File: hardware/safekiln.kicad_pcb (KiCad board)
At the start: 2 copper layers, 100 x 70 mm, 125 parts, among them J1 5V DC IN, J10 CT 30A/1V, J11 UART / EXPANSION, J2 USB-C, J3 TC1 KILN (K), J4 Conn_ARM_SWD_TagConnect_TC2030, J5 OLED 128x64 I2C, J6 SSR CTRL, J7 TC2 KILN (K), J8 CONTACTOR COIL 5V, J9 LID SWITCH, Q1 AO3400A, Q3 AO3400A, Q4 AO3400A, Q5 AO3400A, SW1 RESET, SW2 BOOT, SW3 ENCODER, U1 ESP32-S3-WROOM-1, U2 AMS1117-3.3, U3 MAX31856, U4 MAX31856, U5 STM32G031K8Tx

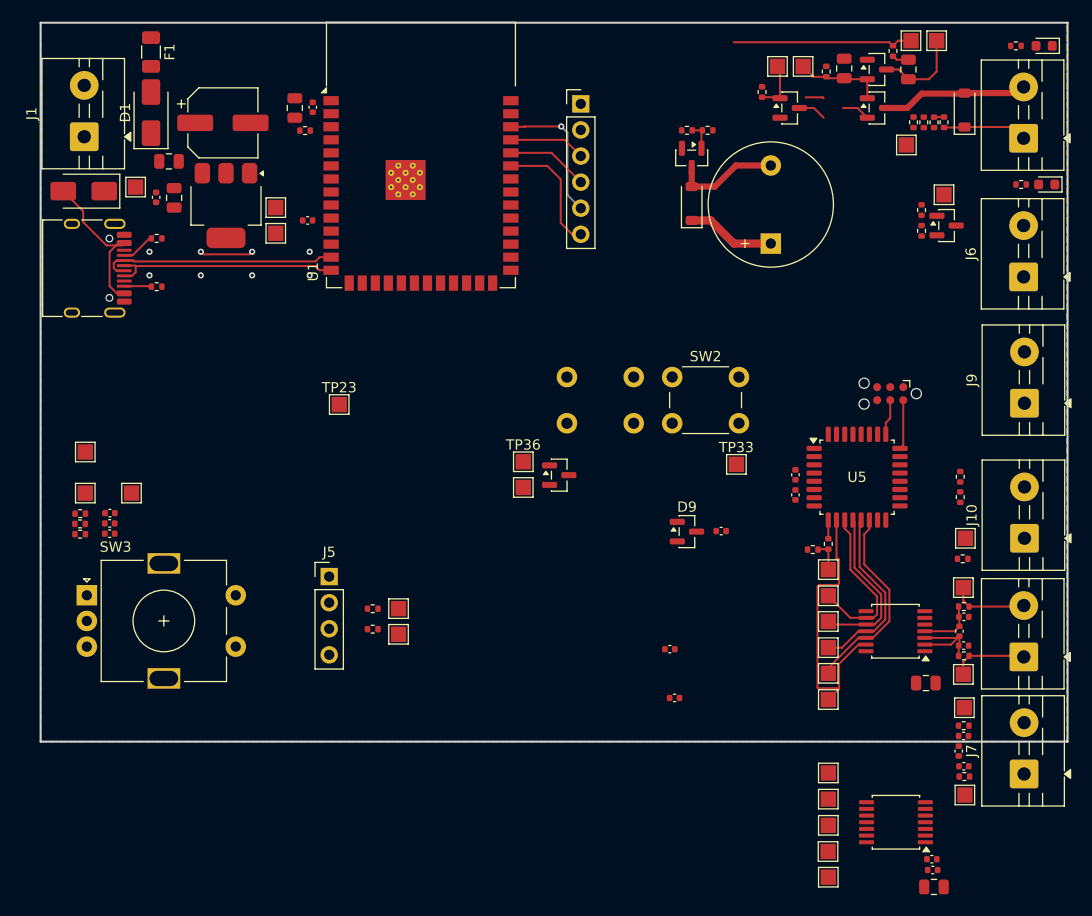
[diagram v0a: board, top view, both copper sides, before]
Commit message: feat: a part number on every bom line, and the buttons go surface mount
Includes the J3/J7 split made in the editor: the two thermocouples are two
2-position blocks again rather than one 4-way, which is what the catalogue
actually stocks. LCSC lists KF301-5.0 in 2P and 3P and no 4P, so the
consolidated connector was a part nobody could order.

All 90 BOM lines now carry an LCSC number, 34 distinct, with the 34 test
points and J4 excluded as the bare pads they are rather than appearing as
lines a BOM cannot fulfil. Three defects came out of doing it:

  R6 and R7 both carried C25076, which is a 100R resistor, while R6 is 220R
  and R7 is 10k. R7 is the pull-up in the supervisor's TX network, so 100R
  would have drawn 33 mA and left R6 no longer limiting anything. One part
  number had propagated onto three different resistance values by field copy.
  Now C25091 and C25744.

  J7 kept J3's value when it was copied, so both thermocouple blocks read
  TC1, on the BOM and on the silkscreen, for a board whose two couples are
  the thing the supervisor cross-checks.

  The 34 test points were (in_bom yes).

Nothing caught any of that because there is no hardware gate in CI at all:
no ERC, no DRC, no BOM check. ERC is clean today at --severity-all with no
exclusions, and tools/fetch3d.py --check verifies the models, so a job
running both plus "every BOM line has an LCSC" and "no part number against
two values" would hold the line at no cost. Tracked as A33.

SW1, SW2 and BZ1 are surface mount. The switches go to the XKB TS-1187A
(C318884), whose footprint KiCad already ships, and neither switch net was
routed yet, so the swap cost no rework. The low-profile 1.5 mm variant is
deliberate: these are service controls, and while RESET also clears the
supervisor's trip latch through D4 (A27), making it easier to press by
accident would be a step backwards.

BZ1 goes to the FST-9650B-5V (C391033), which keeps SYS-HW-09 as written:
active with built-in drive, magnetic, 5 V, and th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
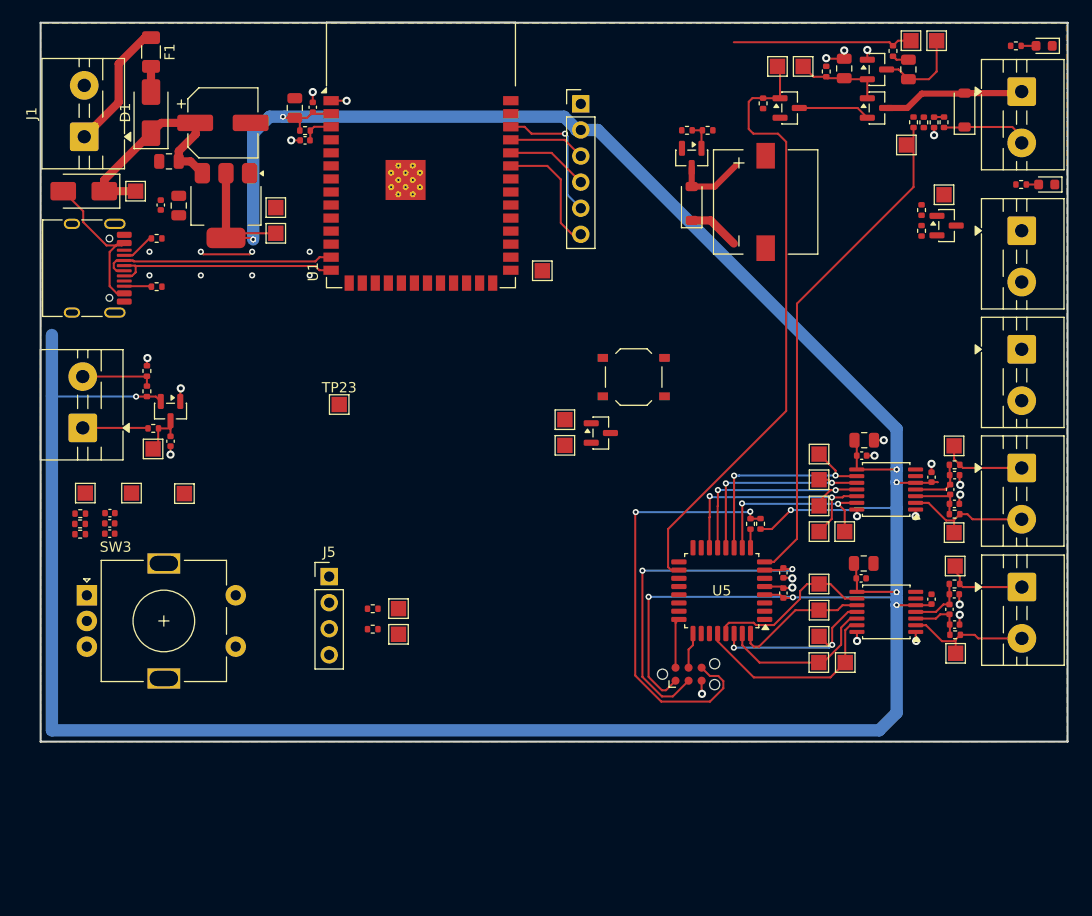
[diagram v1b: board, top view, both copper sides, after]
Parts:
- removed TP35: SUPERVISOR_TX, TestPoint:TestPoint_Pad_1.5x1.5mm
- BZ1: value TMB12A05 5V -> FST-9650B 5V; footprint Buzzer_Beeper:Buzzer_12x9.5RM7.6 -> safekiln:Buzzer_FUET_FST-9650B-5V_9.6x9.6mm
- J3: value TC1 KILN (K) -> TC1
- J7: value TC2 KILN (K) -> TC2
- SW1, SW2: footprint Button_Switch_THT:SW_PUSH_6mm_H5mm -> Button_Switch_SMD:SW_Push_1P1T_XKB_TS-1187A
- moved J10 92.3 mm to (54.1, 79.5)
- moved R25 80.1 mm to (60.4, 73.9), turned to 90 degrees
- moved R26 79.8 mm to (61.0, 79.5)
- moved R24 79.6 mm to (60.4, 75.9), turned to 90 degrees
- moved TP31 79.6 mm to (61.0, 81.5), turned to 180 degrees
- moved C25 54.3 mm to (62.6, 80.8), turned to -90 degrees
- moved D9 51.6 mm to (62.6, 77.8), turned to -90 degrees
- moved J4 33.6 mm to (113.1, 103.4), turned to 0 degrees
- moved C27 32.2 mm to (130.2, 92.7), turned to 0 degrees
- moved C12 30.5 mm to (136.8, 84.2), turned to 90 degrees
- moved C11 29.8 mm to (129.9, 82.2)
- moved C26 29.2 mm to (129.9, 94.1), turned to 0 degrees
- moved TP33 26.7 mm to (98.8, 64.2)
- moved C19 25.3 mm to (136.8, 96.1), turned to 90 degrees
- moved C13 24.4 mm to (130.2, 80.7)
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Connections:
- J3 pad 1: /TC1_N -> /TC1_P
- J3 pad 2: /TC1_P -> /TC1_N
- J7 pad 1: /TC2_N -> /TC2_P
- J7 pad 2: /TC2_P -> /TC2_N
- R29 pad 1: +3.3V -> /COIL_PERMIT
- R29 pad 2: /COIL_PERMIT -> GND
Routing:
- net +3.3V: track 0.00 -> 340.3 mm, vias 0 -> 10
- net /COIL_PERMIT: track 4.99 -> 60.6 mm
- net /COIL_FEEDBACK: track 0.00 -> 48.8 mm
- net /SUPERVISOR_TX: track 3.01 -> 42.3 mm, vias 0 -> 2
- net /SUPERVISOR_RESET: track 0.00 -> 33.8 mm, vias 0 -> 2
- net GND: track 5.21 -> 30.2 mm, vias 8 -> 32
- net /TC2_FAULT: track 0.00 -> 19.7 mm
- net +5V: track 8.63 -> 27.6 mm
- net /TC2_MISO: track 0.00 -> 17.4 mm, vias 0 -> 2
- net /TC2_CS: track 0.00 -> 16.4 mm
- net /TC2_MOSI: track 0.00 -> 15.7 mm
- net /TC2_SCK: track 0.00 -> 13.1 mm
- net /TC2_N: track 0.00 -> 12.7 mm
- net /V_IN: track 0.00 -> 12.7 mm
- net /TC1_FAULT: track 29.7 -> 18.5 mm, vias 0 -> 2
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
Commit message: feat: the board catches up with the 12 V schematic
Update PCB from Schematic, run in the editor: the buck (U2, L1, C28 to C30),
U6, D10, D11, F2, SW4, R36/R37, C31/C32, TP39 and the new footprints for U2,
BZ1, D6, R15 and R21 are on the board. The schematic gains TP4, a second GND
test point, and is otherwise electrically unchanged.

DRC with --schematic-parity: 0 unconnected pads and 0 footprint errors, down
from 61 unconnected pads, so the board and the schematic agree. 209
violations remain, against 232 before, and 199 of them are silkscreen
overlaps. What is left that is not cosmetic:

  J2's stacked VBUS pads (A4/B9 and A9/B4) report as shorts and mask
  bridges, two of each. VBUS is unconnected in the schematic, so each pad
  gets its own "unconnected-" net and the pads that share copper look like
  two nets touching. Naming the net fixes it, and lets U6 pin 5 take VBUS
  as the USBLC6 expects.

  One dangling 0.625 mm +12V stub at 144.1, 55.1, and one starved thermal.

  U1's footprint differs from the RF_Module library copy.

Adds safekiln.kicad_dru, the project's custom design rules, and
safekiln.xml, an IPC-2581 export of the board.
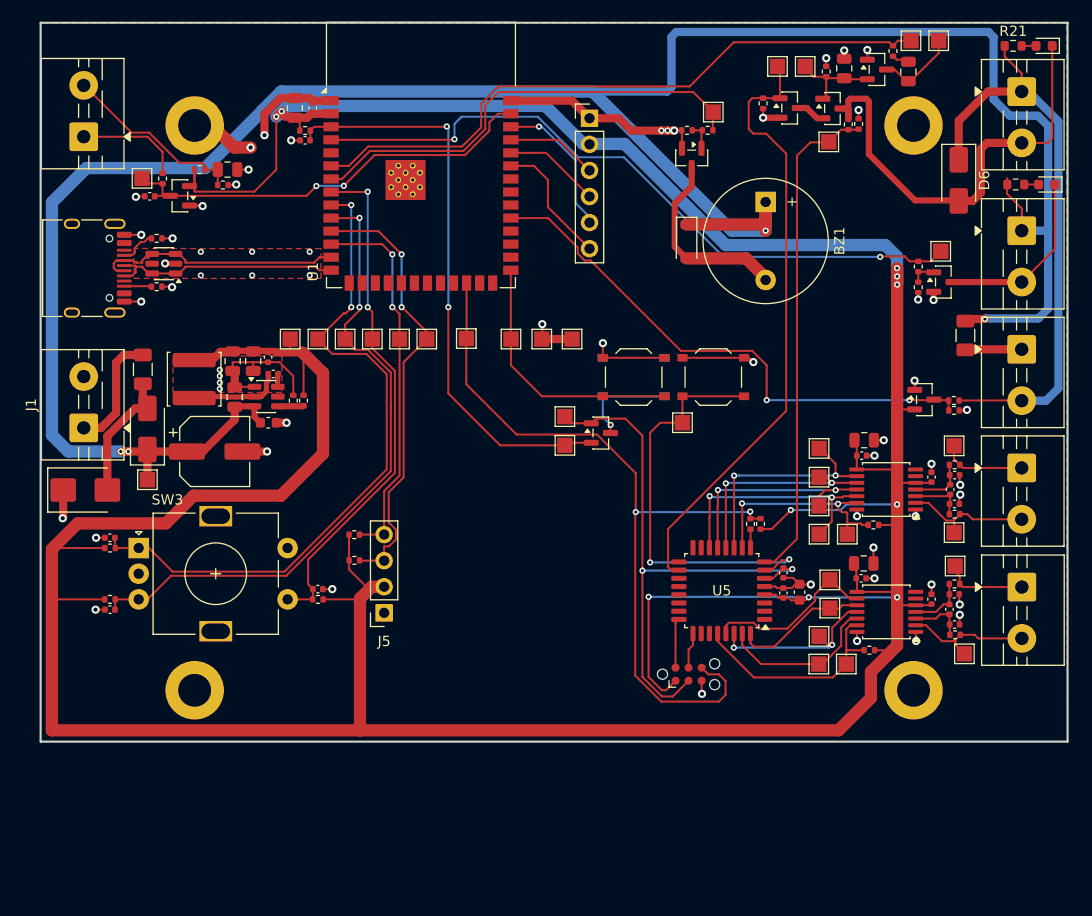
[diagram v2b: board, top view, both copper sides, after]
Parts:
- removed D2: SS34, Diode_SMD:D_SMA
- added C28: 100nF, Capacitor_SMD:C_0402_1005Metric, F.Cu at (72.7, 74.2)
- added C29: 22uF, Capacitor_SMD:C_0805_2012Metric, F.Cu at (68.7, 73.0)
- added C30: 100nF 50V, Capacitor_SMD:C_0603_1608Metric, F.Cu at (72.2, 79.0)
- added C31: 10uF, Capacitor_SMD:C_0805_2012Metric, F.Cu at (68.2, 54.3)
- added C32: 4.7uF, Capacitor_SMD:C_0603_1608Metric, F.Cu at (123.9, 95.5)
- added D10: BAT54S, Package_TO_SOT_SMD:SOT-23, F.Cu at (136.1, 76.7)
- added D11: SMBJ15CA, Diode_SMD:D_SMB, F.Cu at (54.4, 85.5)
- added F2: PTC 0.5A 15V, Fuse:Fuse_1206_3216Metric, F.Cu at (140.1, 70.5)
- added H1: Mount, MountingHole:MountingHole_3.2mm_M3_ISO7380_Pad, F.Cu at (135.0, 50.0)
- added H2: Mount, MountingHole:MountingHole_3.2mm_M3_ISO7380_Pad, F.Cu at (135.0, 105.0)
- added H3: Mount, MountingHole:MountingHole_3.2mm_M3_ISO7380_Pad, F.Cu at (65.0, 105.0)
- added H4: Mount, MountingHole:MountingHole_3.2mm_M3_ISO7380_Pad, F.Cu at (65.0, 50.0)
- added L1: 10uH, Inductor_SMD:L_Sunlord_SWPA5040S, F.Cu at (65.0, 74.7)
- added R34: 100k, Resistor_SMD:R_0402_1005Metric, F.Cu at (75.6, 76.8)
- added R35: 22.1k, Resistor_SMD:R_0402_1005Metric, F.Cu at (74.6, 76.8)
- added R36: 10k, Resistor_SMD:R_0402_1005Metric, F.Cu at (131.1, 88.9)
- added R37: 10k, Resistor_SMD:R_0402_1005Metric, F.Cu at (130.7, 101.1)
- added SW4: CLEAR, Button_Switch_SMD:SW_Push_1P1T_XKB_TS-1187A, F.Cu at (115.5, 74.5)
- added TP35: SUPERVISOR_TX, TestPoint:TestPoint_Pad_1.5x1.5mm, F.Cu at (91.5, 70.8)
- added TP39: SUP_CLEAR, TestPoint:TestPoint_Pad_1.5x1.5mm, F.Cu at (112.5, 79.0)
- added TP4: GND, TestPoint:TestPoint_Pad_1.5x1.5mm, F.Cu at (101.8, 70.8)
- added U6: USBLC6-2SC6, Package_TO_SOT_SMD:SOT-23-6, F.Cu at (62.0, 63.5)
- BZ1: value FST-9650B 5V -> TMB12A12; footprint safekiln:Buzzer_FUET_FST-9650B-5V_9.6x9.6mm -> Buzzer_Beeper:Buzzer_12x9.5RM7.6
- C1: value 100uF 16V -> 100uF 25V
- C3: value 10uF -> 22uF
- D6: value 1N4148W -> SS14; footprint Diode_SMD:D_SOD-123 -> Diode_SMD:D_SMA
- F1: value PTC 1.5A -> PTC 1.1A 16V
- J1: value 5V DC IN -> 12V DC IN
- J5: footprint Connector_PinHeader_2.54mm:PinHeader_1x04_P2.54mm_Vertical -> Connector_PinSocket_2.54mm:PinSocket_1x04_P2.54mm_Vertical
- J8: value CONTACTOR COIL 5V -> CONTACTOR COIL 12V
- R15, R21: value 1k -> 2.2k; footprint Resistor_SMD:R_0402_1005Metric -> Resistor_SMD:R_0603_1608Metric
- R30: value 10k -> 22k
- R31, R33: value 18k -> 10k
- R32: value 10k -> 33k
- TP1: value +5V -> +12V
- U2: value AMS1117-3.3 -> TPS54202DDCR; footprint Package_TO_SOT_SMD:SOT-223-3_TabPin2 -> Package_TO_SOT_SMD:SOT-23-6
- moved TP23 46.2 mm to (115.5, 48.7)
- moved C1 32.0 mm to (67.0, 81.8)
- moved F1 30.9 mm to (60.0, 73.8)
- moved D1 30.8 mm to (60.4, 79.5)
- moved TP3 28.9 mm to (98.8, 70.8)
- moved TP16 28.9 mm to (87.6, 70.8), turned to 90 degrees
- moved J10 28.4 mm to (54.2, 51.1)
- moved J1 28.4 mm to (54.2, 79.5)
- moved TP1 28.1 mm to (60.4, 84.5)
- moved R31 28.1 mm to (138.9, 77.8), turned to 0 degrees
- moved TP24 27.2 mm to (77.0, 70.8)
- moved R30 27.1 mm to (138.9, 76.8), turned to 180 degrees
- moved TP31 26.4 mm to (59.9, 55.1), turned to 90 degrees
- moved TP15 26.3 mm to (85.0, 70.8), turned to 90 degrees
- moved TP25 25.6 mm to (79.7, 70.8)
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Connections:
- BZ1 pad 1: +5V -> +12V
- C1 pad 1: +5V -> +12V
- C2 pad 1: +5V -> +12V
- D1 pad 1: +5V -> +12V
- D8 pad 1: +5V -> +12V
- J2 pad A4: /VBUS -> unconnected-(J2-VBUS-PadA4)_1
- J2 pad A9: /VBUS -> unconnected-(J2-VBUS-PadA4)_3
- J2 pad B4: /VBUS -> unconnected-(J2-VBUS-PadA4)
- J2 pad B9: /VBUS -> unconnected-(J2-VBUS-PadA4)_2
- J6 pad 1: +5V -> +12V
- J9 pad 1: +5V -> Net-(J9-Pin_1)
- R15 pad 1: +5V -> +12V
- R21 pad 1: +5V -> /LID_SWITCH
- TP1 pad 1: +5V -> +12V
- U2 pad 2: +3.3V -> Net-(U2-SW)
- U2 pad 3: +5V -> +12V
- U5 pad 6: unconnected-(U5-PF2-Pad6) -> /SUPERVISOR_RESET
- U5 pad 7: /SUPERVISOR_RESET -> /SUP_CLEAR
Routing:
- net +12V: track 0.00 -> 234.8 mm, vias 0 -> 4
- net GND: track 30.2 -> 118.0 mm, vias 32 -> 59
- net +3.3V: track 340.3 -> 411.2 mm
- net /SSR: track 0.00 -> 67.5 mm, vias 0 -> 2
- net /ENC_A: track 0.00 -> 66.5 mm, vias 0 -> 2
- net /ENC_B: track 0.00 -> 63.7 mm, vias 0 -> 2
- net /ESP32_EN: track 3.14 -> 56.6 mm, vias 0 -> 2
- net /LID_SENSE: track 0.97 -> 53.3 mm, vias 0 -> 2
- net /ENC_BTN: track 0.00 -> 50.5 mm, vias 0 -> 2
- net /LID_SWITCH: track 8.23 -> 57.2 mm
- net /HEAT_EN: track 17.6 -> 63.1 mm
- net /ALARM: track 0.00 -> 44.7 mm
- net /I2C_SCL: track 0.00 -> 43.7 mm, vias 0 -> 2
- net /SUP_CLEAR: track 0.00 -> 41.3 mm, vias 0 -> 2
- net /I2C_SDA: track 0.00 -> 37.0 mm, vias 0 -> 2
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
